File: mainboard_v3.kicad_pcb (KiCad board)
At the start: 4 copper layers, 148.6 x 88.9 mm, 37 parts, among them J1 PWR_IN, J3 PLD, J4 PLD, J5 IO, J6 IO, J7 DEBUG, SW1 RESET, U1 W65C02SxP, U2 CY62256-70PC, U3 28C256, U4 DS1813, U5 ATF22V10C, U6 ATF22V10C, U7 W65C22SxP, X1 4Mhz

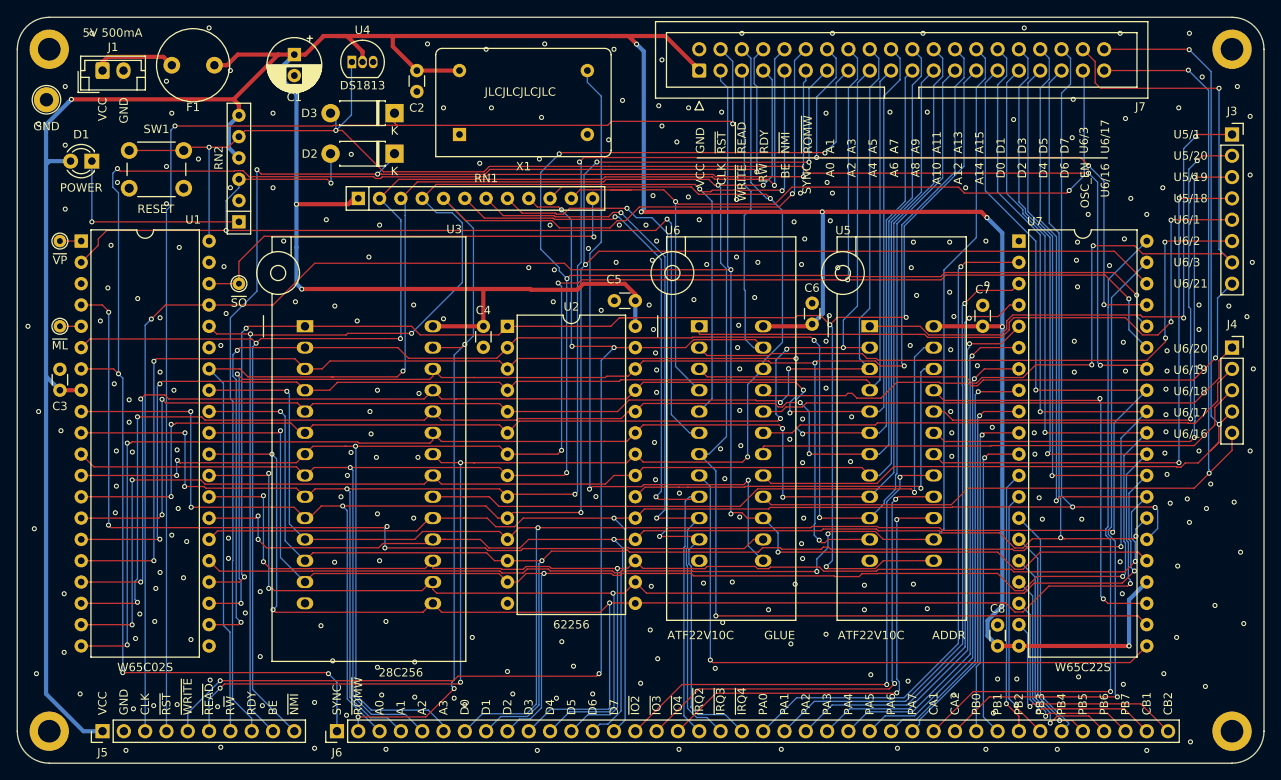
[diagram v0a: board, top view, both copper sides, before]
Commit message: Migrate to KiCad 6
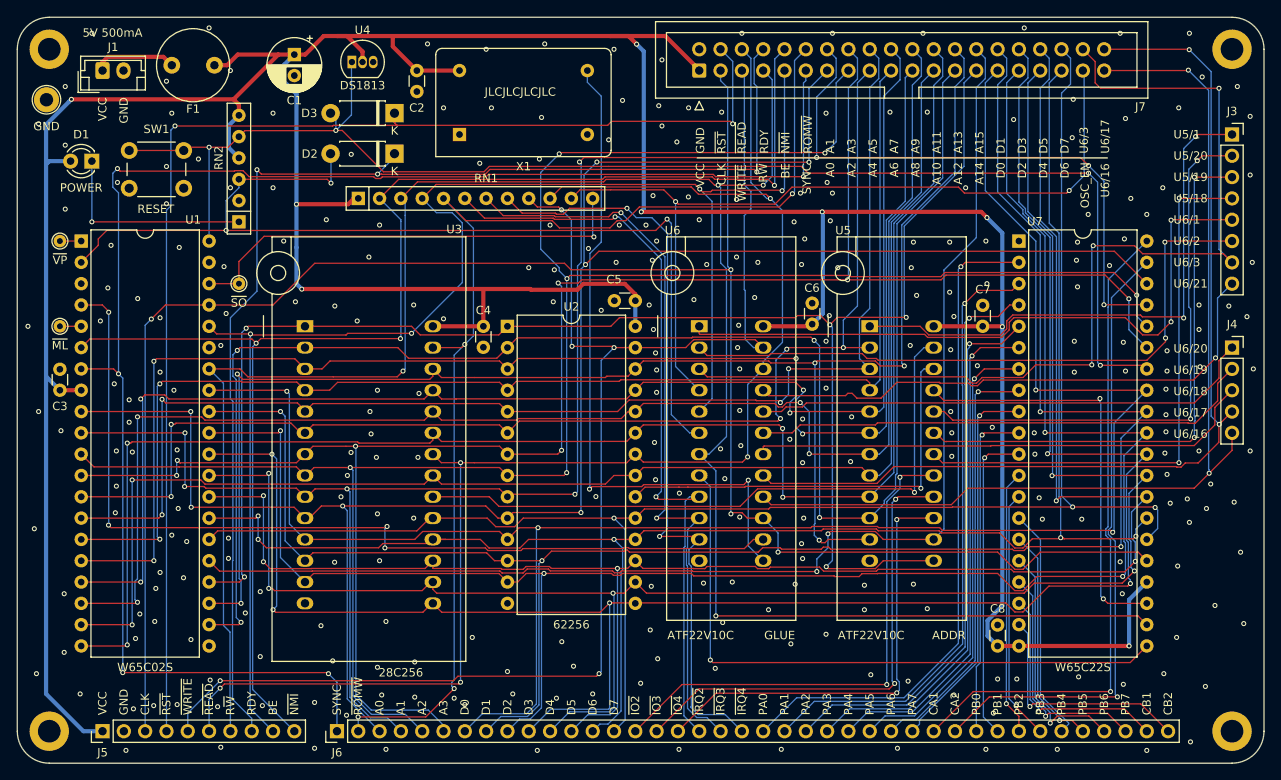
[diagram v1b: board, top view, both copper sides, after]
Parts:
- TP2: value ~ML -> ~{ML}
- TP3: value ~VP -> ~{VP}
- TP4: value ~SO -> ~{SO}
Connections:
- net RAM_~CS renamed RAM_~{CS}
- net ROM_~CS renamed ROM_~{CS}
- net ROM_~WE renamed ROM_~{WE}
- net ~READ renamed ~{READ}
- net ~SO renamed ~{SO}
- net ~WRITE renamed ~{WRITE}
- U1 pad 3: Net-(U1-Pad3) -> unconnected-(U1-Pad3)
- U1 pad 35: Net-(U1-Pad35) -> unconnected-(U1-Pad35)
- U1 pad 39: Net-(U1-Pad39) -> unconnected-(U1-Pad39)
- X1 pad 1: Net-(X1-Pad1) -> unconnected-(X1-Pad1)
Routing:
- net OSC_EN: track 102.9 -> 100.5 mm
- net /a14: track 192.9 -> 191.0 mm
- net U6-17: track 118.9 -> 117.5 mm
- net Net-(F1-Pad2): track 11.0 -> 9.93 mm
- net RDY: track 122.3 -> 121.6 mm
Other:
- net class Default removed
- board text added: "R~{W}"
- board text added: "~{IO2}"
- board text added: "~{IO3}"
- board text added: "~{IO4}"
- board text added: "~{IRQ2}"
- board text added: "~{IRQ3}"
- board text added: "~{IRQ4}"
- board text added: "~{NMI}"
- board text added: "~{READ}"
- board text added: "~{ROMW}"
- board text added: "~{RST}"
- board text added: "~{WRITE}"
- board text removed: "R~W"
- board text removed: "~IO2"
- board text removed: "~IO3"
- board text removed: "~IO4"
- board text removed: "~IRQ2"
- board text removed: "~IRQ3"
- board text removed: "~IRQ4"
- board text removed: "~NMI"
- board text removed: "~READ"
- board text removed: "~ROMW"
- board text removed: "~RST"
- board text removed: "~WRITE"

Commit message: Update
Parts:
- TP2: value ~{ML} -> ~ML
- TP3: value ~{VP} -> ~VP
- TP4: value ~{SO} -> ~SO
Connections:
- net BE renamed /BE
- net CA1 renamed /CA1
- net CA2 renamed /CA2
- net CB1 renamed /CB1
- net CB2 renamed /CB2
- net CLK renamed /CLK
- net IO1 renamed /IO1
- net IO2 renamed /IO2
- net IO3 renamed /IO3
- net IO4 renamed /IO4
- net IRQ renamed /IRQ
- net IRQ1 renamed /IRQ1
- net IRQ2 renamed /IRQ2
- net IRQ3 renamed /IRQ3
- net IRQ4 renamed /IRQ4
- net NMI renamed /NMI
- net OSC renamed /OSC
- net OSC_EN renamed /OSC_EN
- net PA0 renamed /PA0
- net PA1 renamed /PA1
- net PA2 renamed /PA2
- net PA3 renamed /PA3
- net PA4 renamed /PA4
- net PA5 renamed /PA5
- net PA6 renamed /PA6
- net PA7 renamed /PA7
- net PB0 renamed /PB0
- net PB1 renamed /PB1
- net PB2 renamed /PB2
- net PB3 renamed /PB3
- net PB4 renamed /PB4
- net PB5 renamed /PB5
- net PB6 renamed /PB6
- net PB7 renamed /PB7
- net RAM_~{CS} renamed /RAM_~{CS}
- net RDY renamed /RDY
- net RDY_I renamed /RDY_I
- net ROM_~{CS} renamed /ROM_~{CS}
- net ROM_~{WE} renamed /ROM_~{WE}
- net RST renamed /RST
- net RST_I renamed /RST_I
- net RW renamed /RW
- net SYNC renamed /SYNC
- net U5-1 renamed /U5-1
- net U5-18 renamed /U5-18
- net U5-19 renamed /U5-19
- net U5-20 renamed /U5-20
- net U6-1 renamed /U6-1
- net U6-16 renamed /U6-16
- net U6-17 renamed /U6-17
- net U6-18 renamed /U6-18
- net U6-19 renamed /U6-19
- net U6-2 renamed /U6-2
- net U6-20 renamed /U6-20
- net U6-21 renamed /U6-21
- net U6-3 renamed /U6-3
- net ~{READ} renamed /~{READ}
- net ~{SO} renamed /~{SO}
- net ~{WRITE} renamed /~{WRITE}
